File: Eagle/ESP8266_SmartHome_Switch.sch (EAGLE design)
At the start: 1 part

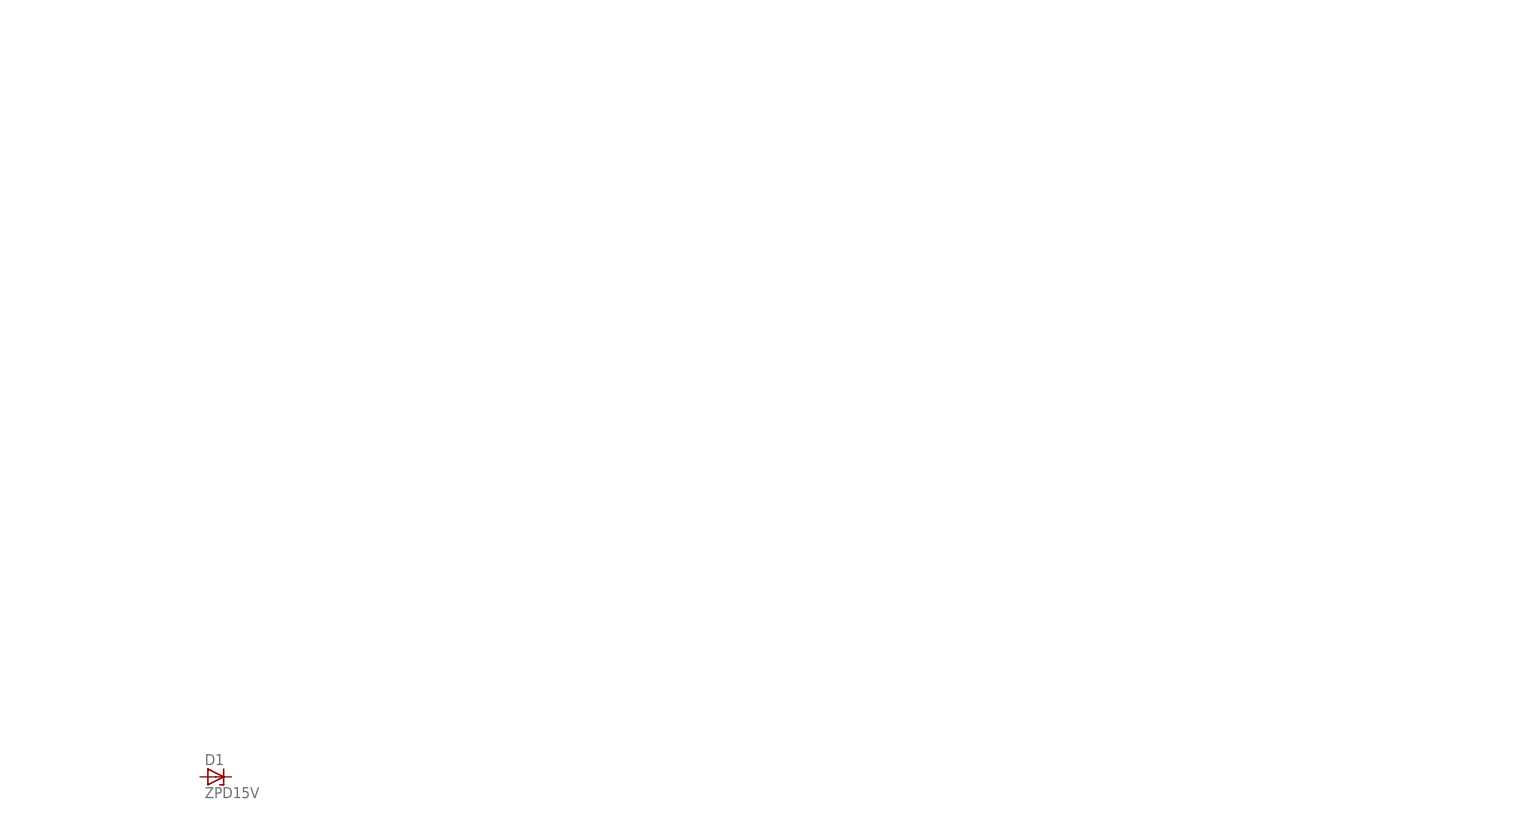
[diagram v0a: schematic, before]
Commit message: Finish power part of ESP8266 SmartHome switch
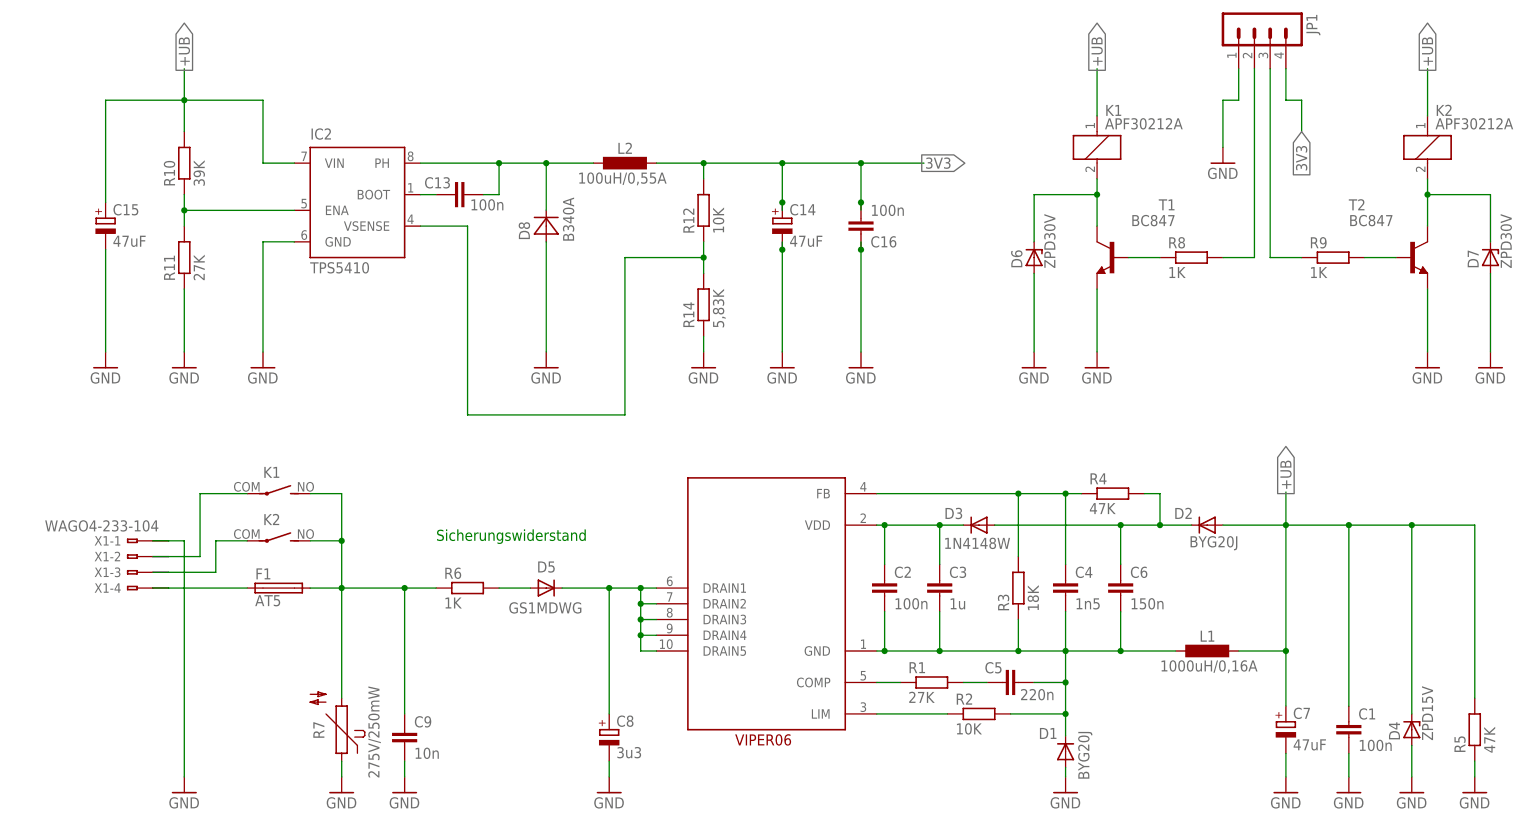
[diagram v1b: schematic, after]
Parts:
- added C1, C13, C16, C2: 100n, resistor:C-EUC0603
- added C14, C15, C7: 47uF, rcl:CPOL-EUD/7343-31W
- added C3: 1u, resistor:C-EUC0603
- added C4: 1n5, resistor:C-EUC0603
- added C5: 220n, resistor:C-EUC0603
- added C6: 150n, resistor:C-EUC0603
- added C8: 3u3, rcl:CPOL-EUE5-10.5
- added C9: 10n, capacitor-wima:C7.5/4
- added D2: BYG20J, diode:DIODE-DO-214AC
- added D3: 1N4148W, diode:CGRM4001-G
- added D4: ZPD15V, diode:ZENER-DIODESMB
- added D5: GS1MDWG, diode:DIODE-DO214AC
- added D6, D7: ZPD30V, diode:ZENER-DIODESMB
- added D8: B340A, diode:MBRA340T3
- added F1: AT5, fuse:TR5
- added IC1: VIPER06HS, SmartHome_Switch_Parts:VIPER06HS
- added IC2: TPS5410, texas:TPS5410
- added JP1: (no value), con-lstb:MA04-1
- added K1, K2: APF30212A, relay:APF30212A
- added L1: 1000uH/0,16A, resistor:L-EUWE-TPC
- added L2: 100uH/0,55A, resistor:L-EUWE-TPC
- added R1, R11: 27K, resistor:R-EU_R0603
- added R10: 39K, resistor:R-EU_R0603
- added R12, R2: 10K, resistor:R-EU_R0603
- added R14: 5,83K, resistor:R-EU_R0603
- added R3: 18K, resistor:R-EU_R0603
- added R4, R5: 47K, resistor:R-EU_R0603
- added R6: 1K, rcl:R-EU_0414/5V
- added R7: 275V/250mW, varistor:S07K275
- added R8, R9: 1K, resistor:R-EU_R0603
- added T1, T2: BC847, transistor:BC847
- added X1: WAGO4-233-104, con-wago:WAGO4-233-104
- D1: value ZPD15V -> BYG20J; device diode:ZPD -> diode:DIODE-DO-214AC
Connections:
- new net +UB: C1.1, C15.+, C7.+, D2.A, D4.C, IC2.VIN, K11.1, K21.1, L1.1, R10.2, R5.2
- new net 3V3: C14.+, C16.2, JP1.4, L2.1, R12.2
- new net GND: C1.2, C14.-, C15.-, C16.1, C7.-, C8.-, C9.2, D1.A, D4.A, D6.A, D7.A, D8.A, IC2.GND, JP1.1, R11.1, R14.1, R5.1, R7.1, T1.E, T2.E, X1-1.A1, X1-1.B1
- new net N$1: IC1.LIM, R2.1
- new net N$10: C9.1, F1.2, K12.S, K22.S, R6.1, R7.2
- new net N$11: D6.C, K11.2, T1.C
- new net N$12: K12.P, X1-2.A1, X1-2.B1
- new net N$13: K22.P, X1-3.A1, X1-3.B1
- new net N$14: F1.1, X1-4.A1, X1-4.B1
- new net N$15: JP1.2, R8.2
- new net N$16: D7.C, K21.2, T2.C
- new net N$17: R9.2, T2.B
- new net N$18: JP1.3, R9.1
- new net N$19: R8.1, T1.B
- new net N$2: IC1.COMP, R1.1
- new net N$20: IC2.ENA, R10.1, R11.2
- new net N$21: C13.1, IC2.BOOT
- new net N$22: C13.2, D8.C, IC2.PH, L2.2
- new net N$24: IC2.VSENSE, R12.1, R14.2
- new net N$3: C5.1, R1.2
- new net N$4: C2.2, C3.2, C4.2, C5.2, C6.2, D1.C, IC1.GND, L1.2, R2.2, R3.1
- new net N$5: C2.1, C3.1, D3.C, IC1.VDD
- new net N$6: C4.1, IC1.FB, R3.2, R4.1
- new net N$7: C6.1, D2.C, D3.A, R4.2
- new net N$8: C8.+, D5.C, IC1.DRAIN1, IC1.DRAIN2, IC1.DRAIN3, IC1.DRAIN4, IC1.DRAIN5
- new net N$9: D5.A, R6.2
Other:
- note added: "Sicherungswiderstand"
